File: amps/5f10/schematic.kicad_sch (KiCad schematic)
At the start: 42 parts, among them T1 PP OT

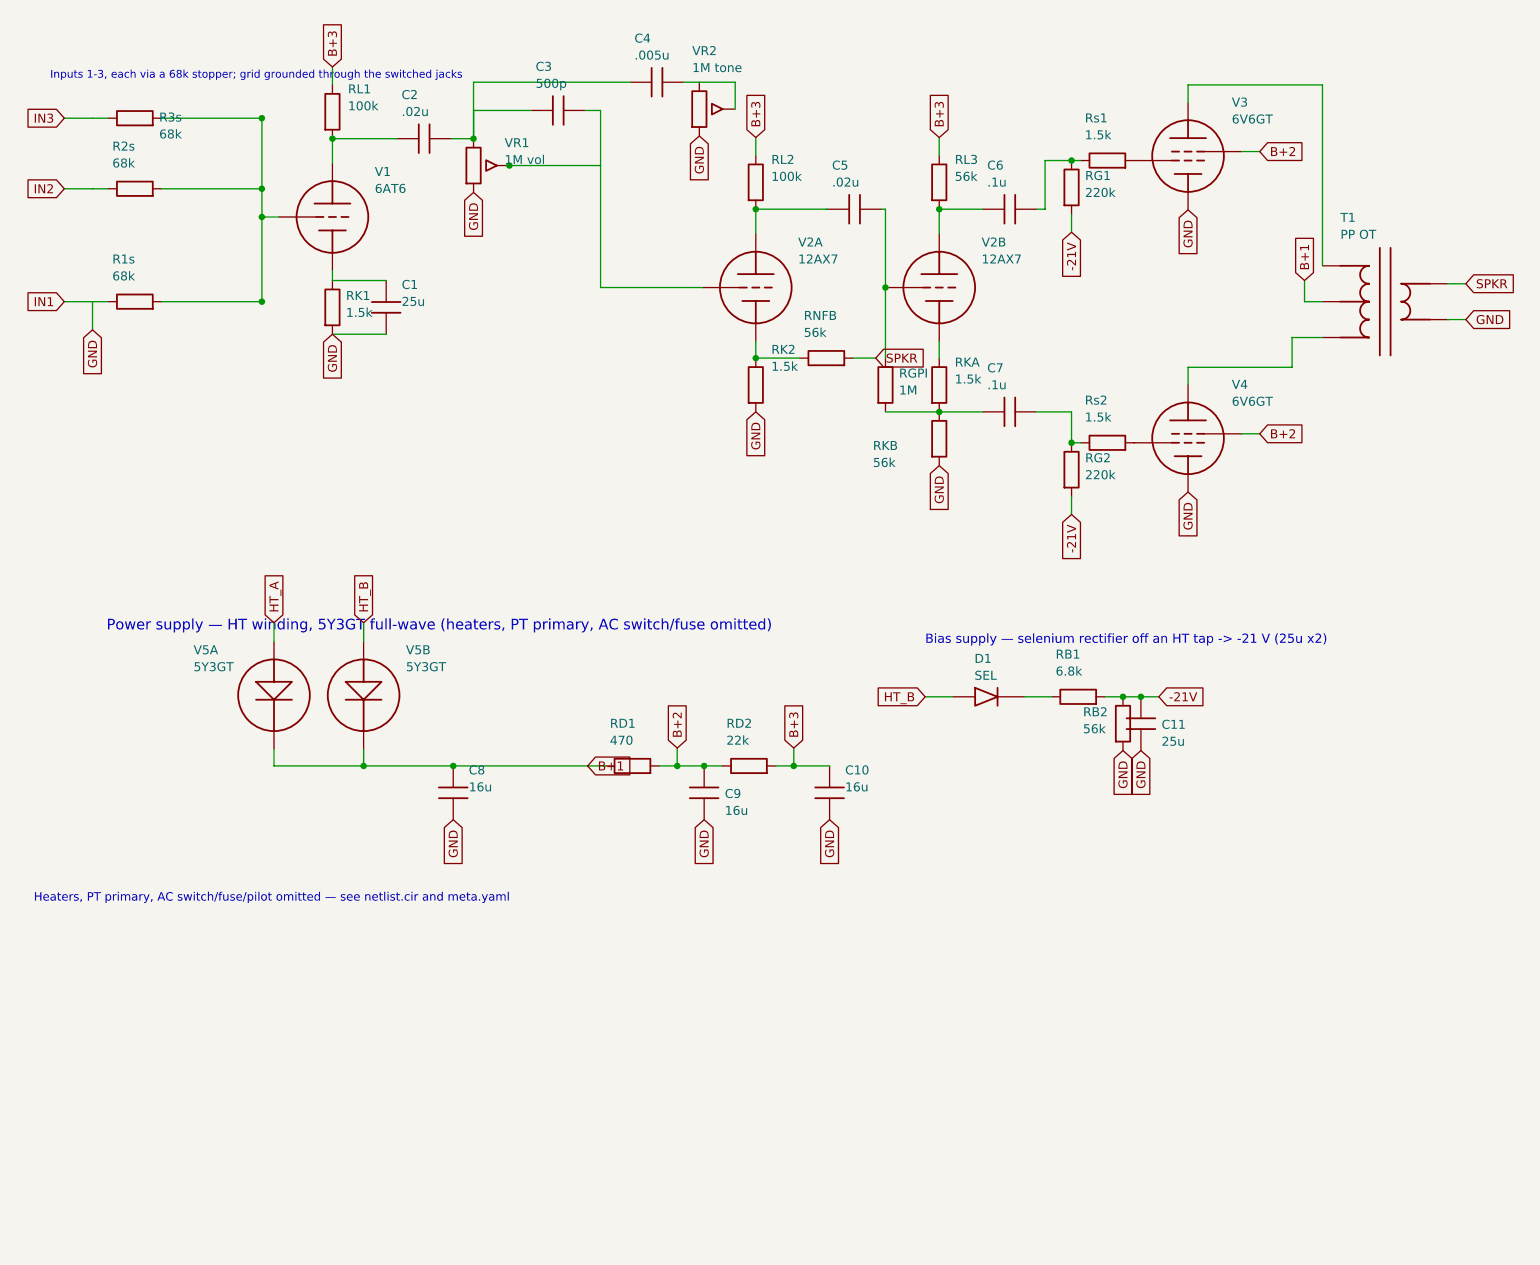
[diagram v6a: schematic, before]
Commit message: Add: real tube pin numbers and readable valve glyphs on every schematic
Phase B of the drawing program. A factory service sheet numbers every tube
pin, because the number is what a technician puts a probe on. This corpus
printed none, and the numbers hidden in its symbols were positional
placeholders (P=1, G=2, K=3) that would have published a 6V6GT's plate as
pin 1 when it is pin 3.

1055 electrodes now carry the real number, 1027 lettered (27 are shared
filaments deduped, 1 dropped for want of clear space on the 6G2). Resolved per
instance from reference/tubes/<slug>.yaml through the same alias resolution the
layout renderer uses, so a 12AX7 section and a 6SL7 section each get their own
basing. A valve whose basing the corpus does not carry prints nothing rather
than a wrong number.

Section letters and basing units are now separate things, which cost a detour
worth recording. The RCA 12AX7-A sheet reads "Pin 1 - Plate of Unit No.2 ...
Pin 6 - Plate of Unit No.1", so unit numbering is not pin order; the 5Y3 and
GZ34 number their units in opposite pin order, so nothing positional can
express it. But the section LETTER is a designator, not a basing fact: this
corpus, like every technician, calls the first stage in signal order V1A, and
five amps' prose already did. On four amps the factory sheets put that first
stage on the other half -- the AA764's own schematic prints +200 V on pin 1 --
so those drawings now state their unit explicitly, each citing its source, and
no letter, netlist, parts list or layout comment changed. 183 layout comments
agree with the printed numbers, 0 disagree. A guard fires if two halves of one
bottle resolve to the same unit, which is exactly how this was found.

Glyphs: the cathode gains a bracket and filament hairpin so it can no longer be
confused with the plate bar, the pentode's screen sits on its own row, and a
rectifier draws as one envelope over its sections instead of two apparent
bottles. Line weights are scaled per sheet to a co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
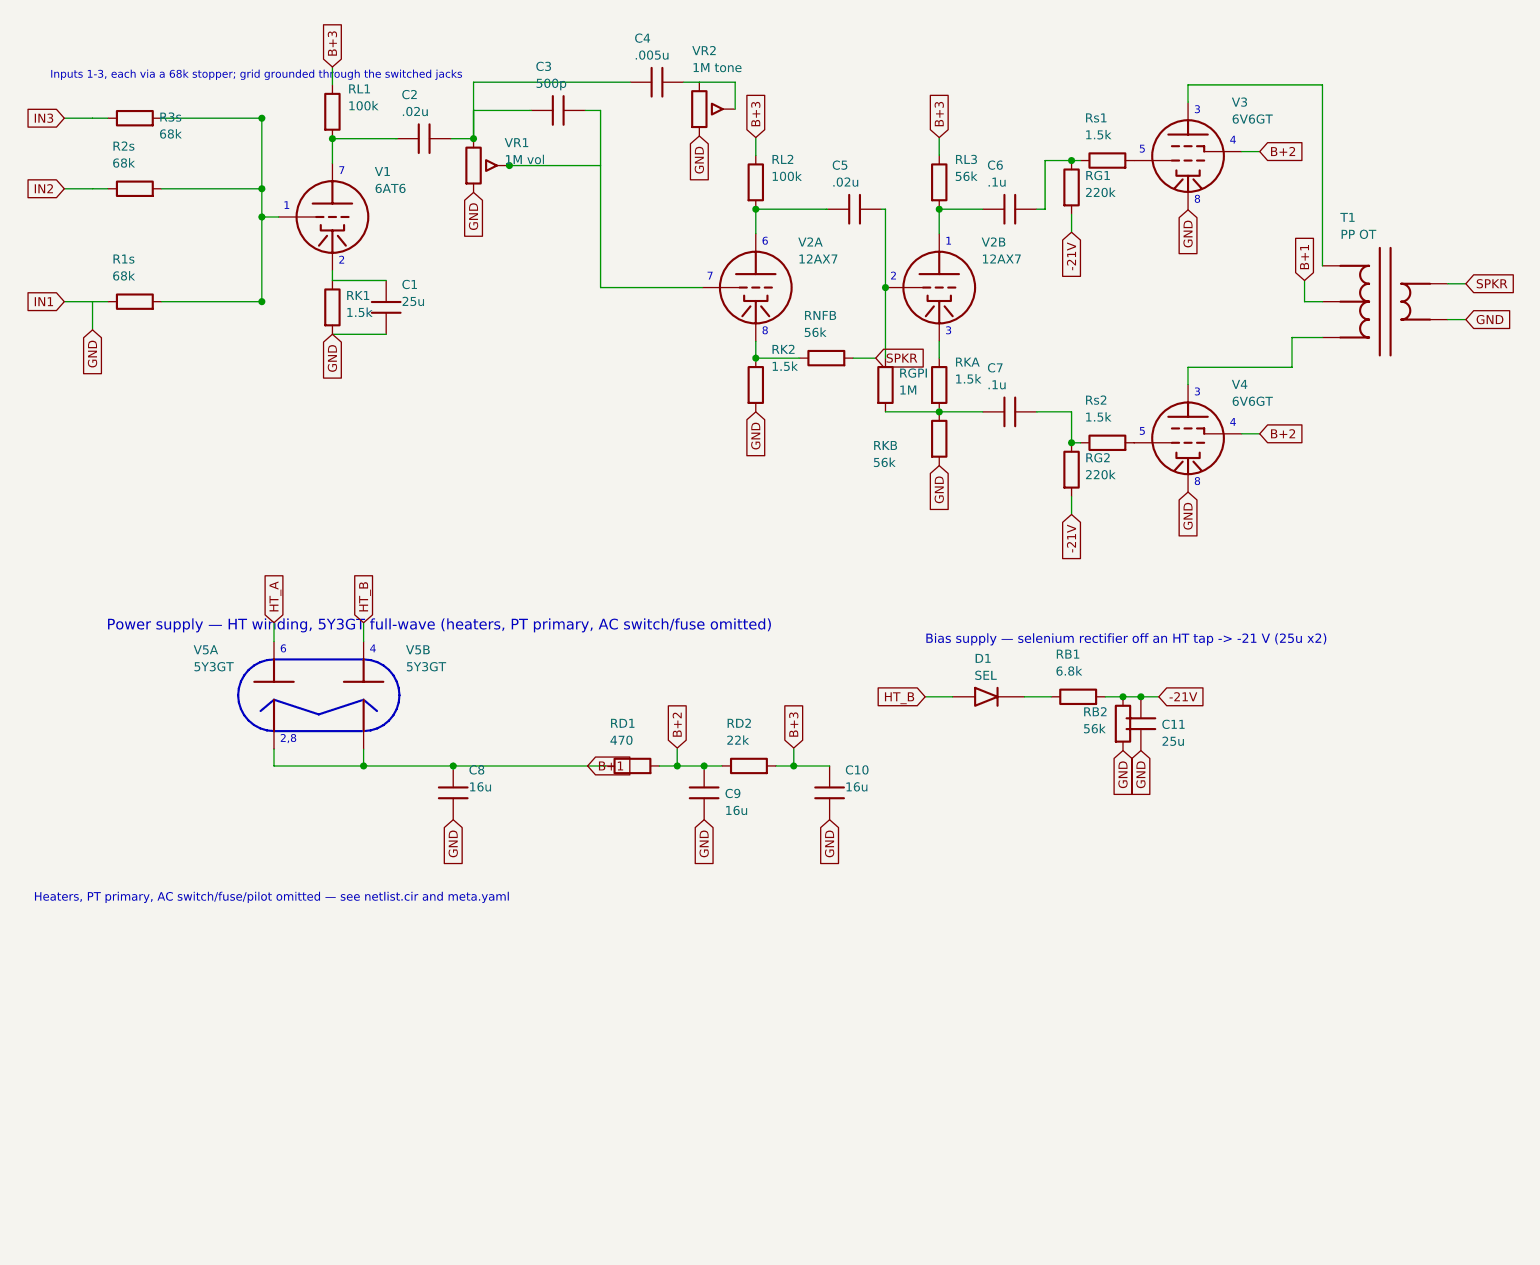
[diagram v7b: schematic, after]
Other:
- note added: "1"
- note added: "2"
- note added: "2,8"
- note added: "3"
- note added: "4"
- note added: "5"
- note added: "6"
- note added: "7"
- note added: "8"
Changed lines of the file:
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@@
   (wire (pts (xy 30.828 24.889) (xy 45.018 24.889))
     (stroke (width 0) (type default)))
-  (junction (at 45.018 24.889) (diameter 0) (color 0 0 0 0))
+  (junction (at 45.018 24.889) (diameter 1) (color 0 0 0 0))
   (global_label "IN2" (shape input) (at 17.018 34.889 180)
     (effects (font (size 1.27 1.27)) (justify right)))
@@
   (wire (pts (xy 30.828 34.889) (xy 45.018 34.889))
     (stroke (width 0) (type default)))
-  (junction (at 45.018 34.889) (diameter 0) (color 0 0 0 0))
+  (junction (at 45.018 34.889) (diameter 1) (color 0 0 0 0))
   (global_label "IN1" (shape input) (at 17.018 50.889 180)
     (effects (font (size 1.27 1.27)) (justify right)))
@@
   (wire (pts (xy 30.828 50.889) (xy 45.018 50.889))
     (stroke (width 0) (type default)))
-  (junction (at 45.018 50.889) (diameter 0) (color 0 0 0 0))
+  (junction (at 45.018 50.889) (diameter 1) (color 0 0 0 0))
   (global_label "GND" (shape input) (at 21.018 54.889 270)
     (effects (font (size 1.27 1.27)) (justify right)))
@@
   (wire (pts (xy 45.018 38.889) (xy 47.398 38.889))
     (stroke (width 0) (type default)))
-  (junction (at 45.018 38.889) (diameter 0) (color 0 0 0 0))
+  (junction (at 45.018 38.889) (diameter 1) (color 0 0 0 0))
   (wire (pts (xy 55.018 31.269) (xy 55.018 27.789))
     (stroke (width 0) (type default)))
@@
   (wire (pts (xy 55.018 27.789) (xy 64.018 27.789))
     (stroke (width 0) (type default)))
-  (junction (at 55.018 27.789) (diameter 0) (color 0 0 0 0))
+  (junction (at 55.018 27.789) (diameter 1) (color 0 0 0 0))
   (symbol (lib_id "cx:C") (at 68.018 27.789 90) (unit 1)
     (in_bom yes) (on_board yes)
@@
   (wire (pts (xy 80.098 31.599) (xy 93.018 31.599))
     (stroke (width 0) (type default)))
-  (junction (at 80.098 31.599) (diameter 0) (color 0 0 0 0))
+  (junction (at 80.098 31.599) (diameter 1) (color 0 0 0 0))
   (wire (pts (xy 75.018 27.789) (xy 75.018 23.789))
     (stroke (width 0) (type default)))
   (wire (pts (xy 75.018 23.789) (xy 75.018 19.789))
     (stroke (width 0) (type default)))
-  (junction (at 75.018 27.789) (diameter 0) (color 0 0 0 0))
+  (junction (at 75.018 27.789) (diameter 1) (color 0 0 0 0))
   (symbol (lib_id "cx:C") (at 101.018 19.789 90) (unit 1)
     (in_bom yes) (on_board yes)
@@
   (wire (pts (xy 115.018 56.509) (xy 115.018 58.889))
     (stroke (width 0) (type default)))
-  (junction (at 115.018 58.889) (diameter 0) (color 0 0 0 0))
+  (junction (at 115.018 58.889) (diameter 1) (color 0 0 0 0))
   (symbol (lib_id "cx:R") (at 115.018 62.699 0) (unit 1)
     (in_bom yes) (on_board yes)
@@
   (wire (pts (xy 115.018 37.789) (xy 125.018 37.789))
     (stroke (width 0) (type default)))
-  (junction (at 115.018 37.789) (diameter 0) (color 0 0 0 0))
+  (junction (at 115.018 37.789) (diameter 1) (color 0 0 0 0))
   (symbol (lib_id "cx:C") (at 129.018 37.789 90) (unit 1)
     (in_bom yes) (on_board yes)
@@
     (property "Reference" "RKA" (at 143.218 59.499 0) (effects (font (size 1.27 1.27)) (justify left)))
     (property "Value" "1.5k" (at 143.218 61.899 0) (effects (font (size 1.27 1.27)) (justify left))))
-  (junction (at 141.018 66.509) (diameter 0) (color 0 0 0 0))
+  (junction (at 141.018 66.509) (diameter 1) (color 0 0 0 0))
   (symbol (lib_id "cx:R") (at 141.018 70.319 0) (unit 1)
     (in_bom yes) (on_board yes)
@@
   (wire (pts (xy 133.398 48.889) (xy 133.398 58.889))
     (stroke (width 0) (type default)))
-  (junction (at 133.398 48.889) (diameter 0) (color 0 0 0 0))
+  (junction (at 133.398 48.889) (diameter 1) (color 0 0 0 0))
   (symbol (lib_id "cx:R") (at 133.398 62.699 0) (unit 1)
     (in_bom yes) (on_board yes)
@@
   (wire (pts (xy 141.018 37.789) (xy 147.208 37.789))
     (stroke (width 0) (type default)))
-  (junction (at 141.018 37.789) (diameter 0) (color 0 0 0 0))
+  (junction (at 141.018 37.789) (diameter 1) (color 0 0 0 0))
   (symbol (lib_id "cx:C") (at 151.018 37.789 90) (unit 1)
     (in_bom yes) (on_board yes)
@@
   (wire (pts (xy 168.658 30.889) (xy 168.658 30.889))
     (stroke (width 0) (type default)))
-  (junction (at 159.768 30.889) (diameter 0) (color 0 0 0 0))
+  (junction (at 159.768 30.889) (diameter 1) (color 0 0 0 0))
   (symbol (lib_id "cx:R") (at 159.768 34.699 0) (unit 1)
     (in_bom yes) (on_board yes)
@@
   (wire (pts (xy 168.658 70.889) (xy 168.658 70.889))
     (stroke (width 0) (type default)))
-  (junction (at 159.768 70.889) (diameter 0) (color 0 0 0 0))
+  (junction (at 159.768 70.889) (diameter 1) (color 0 0 0 0))
   (symbol (lib_id "cx:R") (at 159.768 74.699 0) (unit 1)
     (in_bom yes) (on_board yes)
@@
   (wire (pts (xy 72.138 116.689) (xy 91.188 116.689))
     (stroke (width 0) (type default)))
-  (junction (at 59.438 116.689) (diameter 0) (color 0 0 0 0))
-  (junction (at 72.138 116.689) (diameter 0) (color 0 0 0 0))
+  (junction (at 59.438 116.689) (diameter 1) (color 0 0 0 0))
+  (junction (at 72.138 116.689) (diameter 1) (color 0 0 0 0))
   (symbol (lib_id "cx:C") (at 72.138 120.499 0) (unit 1)
     (in_bom yes) (on_board yes)
@@
   (wire (pts (xy 107.698 116.689) (xy 110.238 116.689))
     (stroke (width 0) (type default)))
-  (junction (at 103.888 116.689) (diameter 0) (color 0 0 0 0))
+  (junction (at 103.888 116.689) (diameter 1) (color 0 0 0 0))
   (global_label "B+2" (shape input) (at 103.888 114.149 90)
     (effects (font (size 1.27 1.27)) (justify left)))
   (wire (pts (xy 103.888 114.149) (xy 103.888 116.689))
     (stroke (width 0) (type default)))
-  (junction (at 107.698 116.689) (diameter 0) (color 0 0 0 0))
+  (junction (at 107.698 116.689) (diameter 1) (color 0 0 0 0))
   (symbol (lib_id "cx:C") (at 107.698 120.499 0) (unit 1)
     (in_bom yes) (on_board yes)
@@
   (wire (pts (xy 120.398 116.689) (xy 125.478 116.689))
     (stroke (width 0) (type default)))
-  (junction (at 120.398 116.689) (diameter 0) (color 0 0 0 0))
+  (junction (at 120.398 116.689) (diameter 1) (color 0 0 0 0))
   (global_label "B+3" (shape input) (at 120.398 114.149 90)
     (effects (font (size 1.27 1.27)) (justify left)))
@@
   (wire (pts (xy 169.598 106.889) (xy 172.138 106.889))
     (stroke (width 0) (type default)))
-  (junction (at 167.058 106.889) (diameter 0) (color 0 0 0 0))
+  (junction (at 167.058 106.889) (diameter 1) (color 0 0 0 0))
   (symbol (lib_id "cx:R") (at 167.058 110.699 0) (unit 1)
     (in_bom yes) (on_board yes)
@@
   (global_label "GND" (shape input) (at 167.058 114.509 270)
     (effects (font (size 1.27 1.27)) (justify right)))
-  (junction (at 169.598 106.889) (diameter 0) (color 0 0 0 0))
+  (junction (at 169.598 106.889) (diameter 1) (color 0 0 0 0))
   (symbol (lib_id "cx:C") (at 169.598 110.699 0) (unit 1)
     (in_bom yes) (on_board yes)
@@
   (global_label "-21V" (shape input) (at 172.138 106.889 0)
     (effects (font (size 1.27 1.27)) (justify left)))
+  (polyline (pts (xy 59.438 101.589) (xy 60.429 101.687) (xy 61.382 101.976) (xy 62.26 102.445) (xy 63.03 103.077) (xy 63.662 103.847) (xy 64.131 104.725) (xy 64.42 105.678) (xy 64.518 106.669) (xy 64.42 107.66) (xy 64.131 108.613) (xy 63.662 109.491) (xy 63.03 110.261) (xy 62.26 110.893) (xy 61.382 111.362) (xy 60.429 111.651) (xy 59.438 111.749) (xy 46.738 111.749) (xy 45.747 111.651) (xy 44.794 111.362) (xy 43.916 110.893) (xy 43.146 110.261) (xy 42.514 109.491) (xy 42.045 108.613) (xy 41.756 107.66) (xy 41.658 106.669) (xy 41.756 105.678) (xy 42.045 104.725) (xy 42.514 103.847) (xy 43.146 103.077) (xy 43.916 102.445) (xy 44.794 101.976) (xy 45.747 101.687) (xy 46.738 101.589) (xy 59.438 101.589))
+    (stroke (width 0.3) (type default) (color 197 163 255 1)) (fill (type none)))
+  (polyline (pts (xy 44.838 108.904) (xy 46.738 107.304) (xy 53.088 109.384) (xy 59.438 107.304) (xy 61.338 108.904))
+    (stroke (width 0.3) (type default) (color 197 163 255 1)) (fill (type none)))
+  (text "7" (at 55.868 32.539 0)
+    (effects (font (size 1.1 1.1)) (justify left)))
+  (text "1" (at 48.0708 37.489 0)
+    (effects (font (size 1.1 1.1)) (justify left)))
+  (text "2" (at 55.868 45.239 0)
+    (effects (font (size 1.1 1.1)) (justify left)))
+  (text "6" (at 115.868 42.539 0)
+    (effects (font (size 1.1 1.1)) (justify left)))
+  (text "7" (at 108.071 47.489 0)
+    (effects (font (size 1.1 1.1)) (justify left)))
+  (text "8" (at 115.868 55.239 0)
+    (effects (font (size 1.1 1.1)) (justify left)))
+  (text "1" (at 141.868 42.539 0)
+    (effects (font (size 1.1 1.1)) (justify left)))
+  (text "2" (at 134.071 47.489 0)
+    (effects (font (size 1.1 1.1)) (justify left)))
+  (text "3" (at 141.868 55.239 0)
+    (effects (font (size 1.1 1.1)) (justify left)))
+  (text "3" (at 177.128 23.904 0)
+    (effects (font (size 1.1 1.1)) (justify left)))
+  (text "5" (at 169.331 29.489 0)
+    (effects (font (size 1.1 1.1)) (justify left)))
+  (text "4" (at 182.178 28.219 0)
+    (effects (font (size 1.1 1.1)) (justify left)))
+  (text "8" (at 177.128 36.604 0)
+    (effects (font (size 1.1 1.1)) (justify left)))
+  (text "3" (at 177.128 63.904 0)
+    (effects (font (size 1.1 1.1)) (justify left)))
+  (text "5" (at 169.331 69.489 0)
+    (effects (font (size 1.1 1.1)) (justify left)))
+  (text "4" (at 182.178 68.219 0)
+    (effects (font (size 1.1 1.1)) (justify left)))
+  (text "8" (at 177.128 76.604 0)
+    (effects (font (size 1.1 1.1)) (justify left)))
+  (text "6" (at 47.588 100.319 0)
+    (effects (font (size 1.1 1.1)) (justify left)))
+  (text "2,8" (at 47.588 113.019 0)
+    (effects (font (size 1.1 1.1)) (justify left)))
+  (text "4" (at 60.288 100.319 0)
+    (effects (font (size 1.1 1.1)) (justify left)))
   (text "Heaters, PT primary, AC switch/fuse/pilot omitted — see netlist.cir and meta.yaml" (at 12.7 135.467 0)
     (effects (font (size 1.2 1.2)) (justify left)))
